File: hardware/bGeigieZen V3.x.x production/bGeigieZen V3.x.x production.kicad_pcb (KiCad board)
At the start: 2 copper layers, 129.4 x 64.6 mm, 17 parts, among them J1 M5 2x15 pin, J10 QI GND, J11 QI charger Plus, J2 Geiger IRover, J3 GPS, J4 Geiger Safepulse, J5 Extra support header, J6 Grove, J8 QI charger ground, J9 QI Plus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

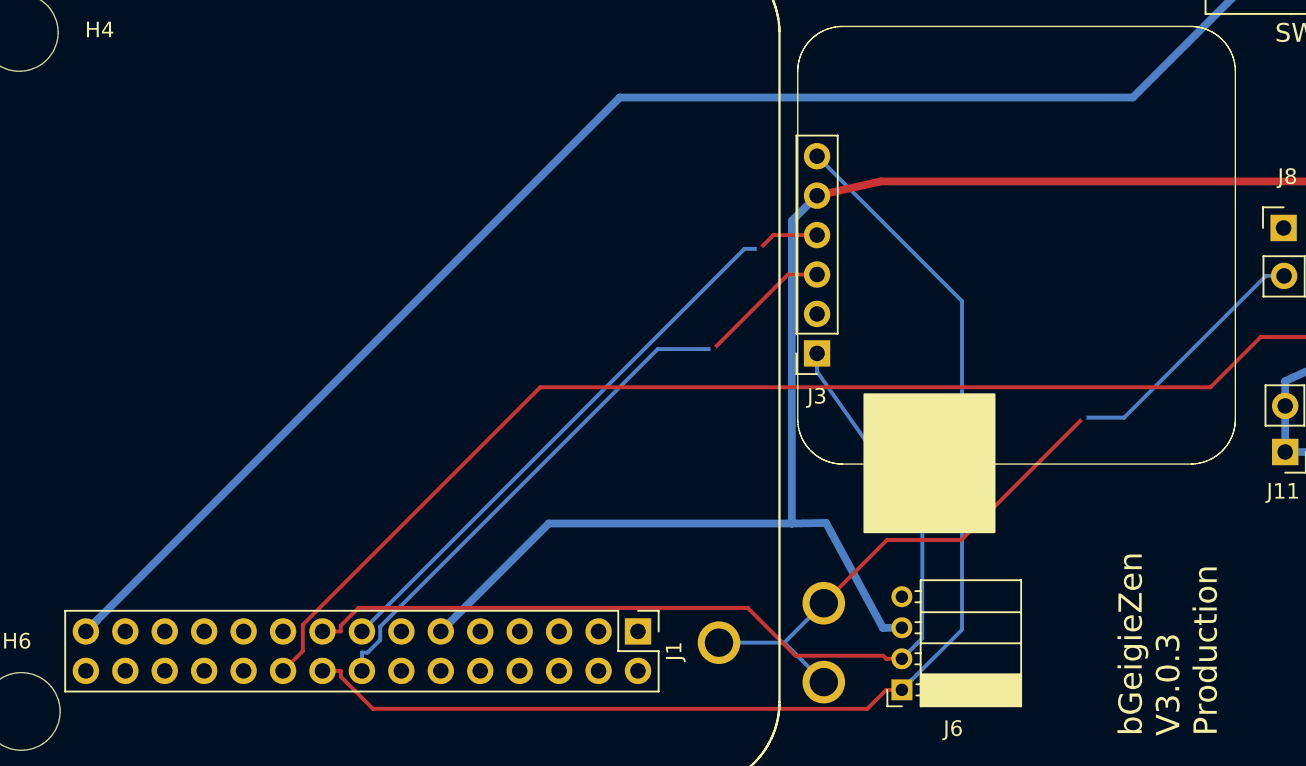
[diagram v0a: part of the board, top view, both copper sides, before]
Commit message: Cleaned up a lot of file. 4.0.1 was a bad board design. :(
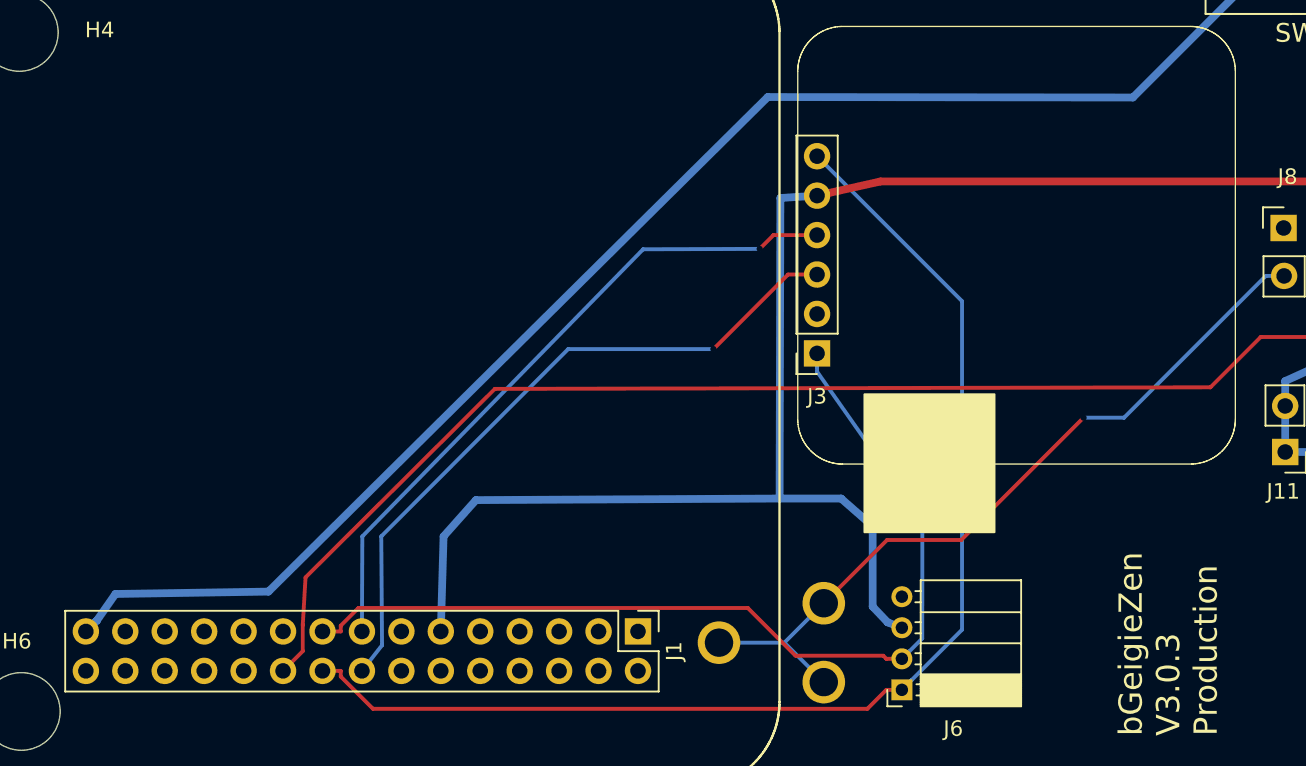
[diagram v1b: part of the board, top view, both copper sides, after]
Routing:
- net 3.3V: track 116.0 -> 122.4 mm
- net /RX2: track 39.9 -> 43.6 mm
- net /TX2: track 41.7 -> 45.1 mm
- net /GIO2 on Core and GIO32 on Core-2: track 107.8 -> 109.4 mm
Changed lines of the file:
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@@
 (kicad_pcb
-	(version 20240108)
+	(version 20240225)
 	(generator "pcbnew")
-	(generator_version "8.0")
+	(generator_version "8.99")
 	(general
 		(thickness 1.6)
@@
 	(segment
 		(start 149.29 91.7701)
-		(end 148.31 91.7701)
+		(end 141.7828 91.7944)
 		(width 0.25)
 		(layer "B.Cu")
@@
 	)
 	(segment
-		(start 123.6726 116.407)
+		(start 123.698 110.2856)
 		(end 123.673 116.407)
 		(width 0.25)
@@
 	)
 	(segment
-		(start 148.31 91.7701)
-		(end 123.673 116.407)
+		(start 123.673 116.407)
+		(end 123.6726 116.407)
+		(width 0.25)
+		(layer "B.Cu")
+		(net 2)
+	)
+	(segment
+		(start 141.7828 91.7944)
+		(end 123.698 110.2856)
 		(width 0.25)
 		(layer "B.Cu")
@@
 	)
 	(segment
-		(start 123.673 118.064)
-		(end 123.673 118.358)
-		(width 0.25)
-		(layer "B.Cu")
-		(net 3)
-	)
-	(segment
-		(start 146.31 98.2225)
-		(end 142.726 98.2225)
+		(start 124.968 117.296)
+		(end 123.6726 118.947)
 		(width 0.25)
 		(layer "B.Cu")
@@
 	)
 	(segment
-		(start 123.673 118.358)
+		(start 123.6726 118.947)
 		(end 123.673 118.6525)
 		(width 0.25)
@@
 	)
 	(segment
-		(start 142.726 98.2225)
-		(end 124.849 116.099)
-		(width 0.25)
-		(layer "B.Cu")
-		(net 3)
-	)
-	(segment
 		(start 123.673 118.6525)
 		(end 123.673 118.947)
@@
 	)
 	(segment
-		(start 124.04 117.77)
-		(end 123.673 117.77)
-		(width 0.25)
-		(layer "B.Cu")
-		(net 3)
-	)
-	(segment
-		(start 123.673 117.77)
-		(end 123.673 118.064)
-		(width 0.25)
-		(layer "B.Cu")
-		(net 3)
-	)
-	(segment
-		(start 124.849 116.961)
-		(end 124.04 117.77)
+		(start 123.673 118.6525)
+		(end 123.6726 118.6529)
 		(width 0.25)
 		(layer "B.Cu")
@@
 	)
 	(segment
-		(start 124.849 116.099)
-		(end 124.849 116.961)
+		(start 136.9568 98.2225)
+		(end 124.9172 110.2856)
 		(width 0.25)
 		(layer "B.Cu")
@@
 	)
 	(segment
-		(start 123.673 118.6525)
-		(end 123.6726 118.6529)
+		(start 146.31 98.2225)
+		(end 136.9568 98.2225)
 		(width 0.25)
 		(layer "B.Cu")
@@
 	)
 	(segment
-		(start 123.673 118.064)
-		(end 123.673 118.358)
+		(start 124.9172 110.2856)
+		(end 124.968 117.296)
 		(width 0.25)
 		(layer "B.Cu")
@@
 	)
 	(segment
-		(start 158.448 116.169)
-		(end 158.4476 116.169)
+		(start 152.985 88.34)
+		(end 152.985 88.3402)
 		(width 0.5)
 		(layer "B.Cu")
@@
 	)
 	(segment
-		(start 151.362 109.457)
-		(end 135.702 109.457)
+		(start 150.5712 107.8472)
+		(end 154.5336 107.8472)
 		(width 0.5)
 		(layer "B.Cu")
@@
 	)
 	(segment
-		(start 128.7526 116.407)
-		(end 128.753 116.407)
+		(start 158.448 116.169)
+		(end 158.4476 116.169)
 		(width 0.5)
 		(layer "B.Cu")
@@
 	)
 	(segment
-		(start 151.362 89.9626)
-		(end 151.362 109.457)
+		(start 128.753 116.407)
+		(end 128.7526 116.407)
 		(width 0.5)
 		(layer "B.Cu")
@@
 	)
 	(segment
-		(start 158.4476 116.169)
-		(end 157.226 116.1784)
+		(start 196.148 90.47)
+		(end 197.749 90.47)
 		(width 0.5)
 		(layer "B.Cu")
@@
 	)
 	(segment
-		(start 196.148 90.47)
-		(end 197.749 90.47)
+		(start 157.5308 115.8228)
+		(end 158.4476 116.169)
 		(width 0.5)
 		(layer "B.Cu")
@@
 	)
 	(segment
-		(start 135.702 109.457)
-		(end 128.753 116.407)
+		(start 156.5656 109.6252)
+		(end 156.5656 114.8068)
+		(width 0.5)
+		(layer "B.Cu")
+		(net 4)
+	)
+	(segment
+		(start 131.0132 107.9488)
+		(end 128.9304 110.2856)
 		(width 0.5)
 		(layer "B.Cu")
@@
 	)
 	(segment
-		(start 157.226 116.1784)
-		(end 153.5684 109.422)
+		(start 150.5712 107.8472)
+		(end 131.0132 107.9488)
 		(width 0.5)
 		(layer "B.Cu")
@@
 	)
 	(segment
-		(start 152.985 88.34)
-		(end 152.985 88.3402)
+		(start 154.5336 107.8472)
+		(end 156.5656 109.6252)
 		(width 0.5)
 		(layer "B.Cu")
@@
 	)
 	(segment
-		(start 153.5684 109.422)
-		(end 151.362 109.457)
+		(start 152.9846 88.34)
+		(end 152.985 88.34)
 		(width 0.5)
 		(layer "B.Cu")
@@
 	)
 	(segment
-		(start 196.148 90.47)
-		(end 196.1476 90.47)
+		(start 150.622 88.4924)
+		(end 150.5712 107.8472)
 		(width 0.5)
 		(layer "B.Cu")
@@
 	)
 	(segment
-		(start 152.985 88.3402)
-		(end 151.362 89.9626)
+		(start 128.9304 110.2856)
+		(end 128.753 116.407)
 		(width 0.5)
 		(layer "B.Cu")
@@
 	)
 	(segment
-		(start 152.9846 88.34)
-		(end 152.985 88.34)
+		(start 196.148 90.47)
+		(end 196.1476 90.47)
+		(width 0.5)
+		(layer "B.Cu")
+		(net 4)
+	)
+	(segment
+		(start 156.5656 114.8068)
+		(end 157.5308 115.8228)
 		(width 0.5)
 		(layer "B.Cu")
@@
 	)
 	(segment
+		(start 152.985 88.3402)
+		(end 150.622 88.4924)
+		(width 0.5)
+		(layer "B.Cu")
+		(net 4)
+	)
+	(segment
 		(start 207.916 117.14)
 		(end 207.9258 117.1498)
@@
 	)
 	(segment
-		(start 181.5572 97.4441)
-		(end 178.3169 100.6844)
+		(start 196.8472 97.4441)
+		(end 181.5572 97.4441)
 		(width 0.25)
 		(layer "F.Cu")
@@
 	)
 	(segment
-		(start 196.8472 97.4441)
-		(end 181.5572 97.4441)
-		(width 0.25)
-		(layer "F.Cu")
-		(net 19)
-	)
-	(segment
-		(start 119.8626 117.677)
-		(end 118.5926 118.947)
+		(start 119.8626 115.9833)
+		(end 119.8626 117.677)
 		(width 0.25)
 		(layer "F.Cu")
@@
 	)
 	(segment
+		(start 120.0404 112.9272)
+		(end 119.8626 115.9833)
+		(width 0.25)
+		(layer "F.Cu")
+		(net 19)
+	)
+	(segment
 		(start 198.1262 96.1651)
 		(end 193.608 91.6467)
@@
 	)
 	(segment
+		(start 119.8626 117.677)
+		(end 118.5926 118.947)
+		(width 0.25)
+		(layer "F.Cu")
+		(net 19)
+	)
+	(segment
 		(start 193.608 91.3521)
 		(end 193.608 91.0583)
@@
 	)
 	(segment
+		(start 198.1262 96.1651)
+		(end 196.8472 97.4441)
+		(width 0.25)
+		(layer "F.Cu")
+		(net 19)
+	)
+	(segment
 		(start 193.608 90.7641)
 		(end 193.6076 90.7637)
@@
 	)
 	(segment
-		(start 178.3169 100.6844)
-		(end 135.1615 100.6844)
-		(width 0.25)
-		(layer "F.Cu")
-		(net 19)
-	)
-	(segment
 		(start 199.831 97.87)
 		(end 198.1262 96.1651)
@@
 	)
 	(segment
-		(start 135.1615 100.6844)
-		(end 119.8626 115.9833)
+		(start 132.2324 100.786)
+		(end 120.0404 112.9272)
 		(width 0.25)
 		(layer "F.Cu")
@@
 	)
 	(segment
-		(start 198.1262 96.1651)
-		(end 196.8472 97.4441)
+		(start 178.3169 100.6844)
+		(end 132.2324 100.786)
 		(width 0.25)
 		(layer "F.Cu")
@@
 	)
 	(segment
-		(start 119.8626 115.9833)
-		(end 119.8626 117.677)
+		(start 181.5572 97.4441)
+		(end 178.3169 100.6844)
 		(width 0.25)
 		(layer "F.Cu")
@@
 	)
 	(segment
-		(start 140.28 82.02)
-		(end 106.613 115.687)
+		(start 149.8092 81.99)
+		(end 117.6528 113.8416)
 		(width 0.5)
 		(layer "B.Cu")
@@
 	)
 	(segment
+		(start 107.7976 113.994)
+		(end 106.613 115.687)
+		(width 0.5)
+		(layer "B.Cu")
+		(net 30)
+	)
+	(segment
 		(start 106.0725 116.227)
 		(end 105.9828 116.317)
@@
 	)
 	(segment
-		(start 181.506 73.8382)
-		(end 181.506 73.8384)
+		(start 181.506 73.8384)
+		(end 173.324 82.02)
+		(width 0.5)
+		(layer "B.Cu")
+		(net 30)
+	)
+	(segment
+		(start 117.6528 113.8416)
+		(end 107.7976 113.994)
 		(width 0.5)
 		(layer "B.Cu")
@@
 	)
 	(segment
+		(start 173.324 82.02)
+		(end 149.8092 81.99)
+		(width 0.5)
+		(layer "B.Cu")
+		(net 30)
+	)
+	(segment
 		(start 106.613 115.687)
 		(end 106.612 115.687)
@@
 	)
 	(segment
-		(start 173.324 82.02)
-		(end 140.28 82.02)
+		(start 181.506 73.8382)
+		(end 181.506 73.8384)
 		(width 0.5)
 		(layer "B.Cu")
@@
 		(width 0.5)
 		(layer "B.Cu")
-		(net 30)
-	)
-	(segment
-		(start 181.506 73.8384)
-		(end 173.324 82.02)
-		(width 0.5)
-		(layer "B.Cu")

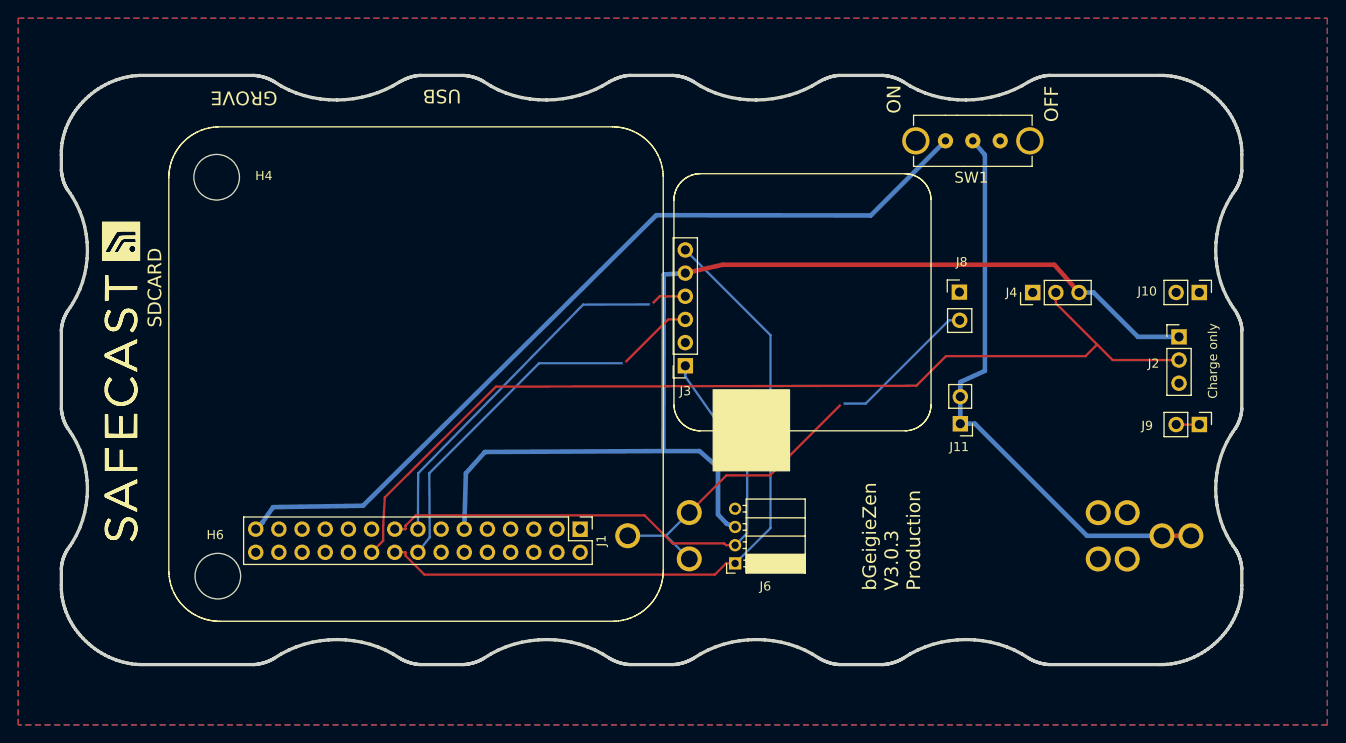
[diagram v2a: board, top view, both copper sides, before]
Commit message: Changed the 18650 battery holder to a 1043 Keystone and modified the layout.
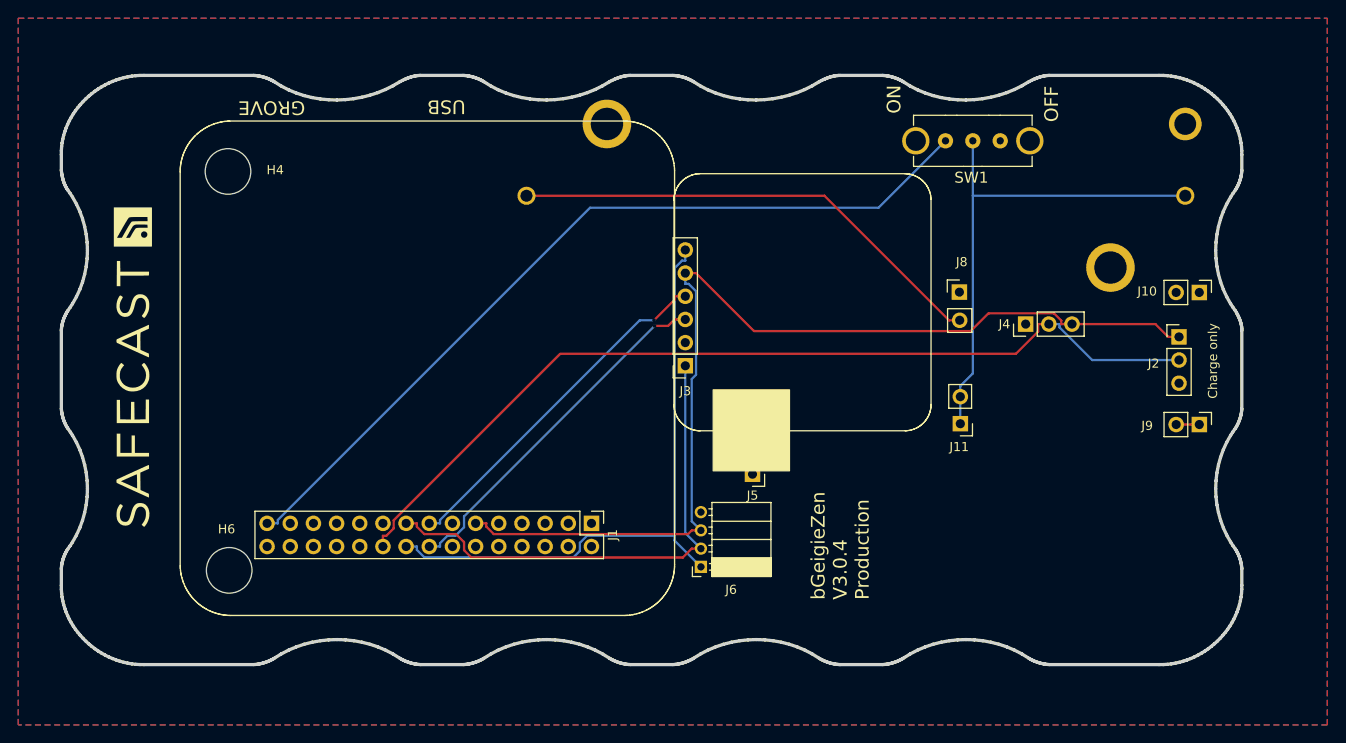
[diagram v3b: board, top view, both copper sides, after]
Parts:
- removed G***: LOGO, bGeigieZen:LOGO
- BT1: footprint Library:BATTERY_18650-HOLDER -> bGeigieZen:1043
- moved BT1 48.2 mm to (207.8, 79.9), turned to 0 degrees
- moved G back 3.83 mm to (92.4, 99.3)
- moved J6 3.77 mm to (154.7, 120.5)
- moved J4 3.54 mm to (190.3, 93.9)
- moved J5 3.54 mm to (160.4, 110.4)
- moved G front 2.04 mm to (92.4, 98.7)
- moved J1 1.40 mm to (142.7, 115.8)
- moved H6 1.40 mm to (103.0, 120.9)
- moved H4 1.40 mm to (102.9, 77.2)
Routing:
- net /SCL: track 79.3 -> 68.3 mm
- net /GIO2 on Core and GIO32 on Core-2: track 109.4 -> 100.9 mm
- net 3.3V: track 122.4 -> 113.9 mm
- net /VBATT: track 63.2 -> 54.9 mm
- net /SDA: track 62.2 -> 55.8 mm
- net /TX2: track 45.1 -> 39.3 mm
- net /RX2: track 43.6 -> 38.8 mm
- net Net-(BT1--): track 49.8 -> 53.1 mm, vias 1 -> 0
- net /BAT: track 94.8 -> 92.0 mm
- net GND: vias 3 -> 0
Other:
- board text added: "bGeigieZen V3.0.4 Production"
- board text removed: "SDCARD"
- board text removed: "bGeigieZen V3.0.3 Production"

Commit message: Added more 3D model files
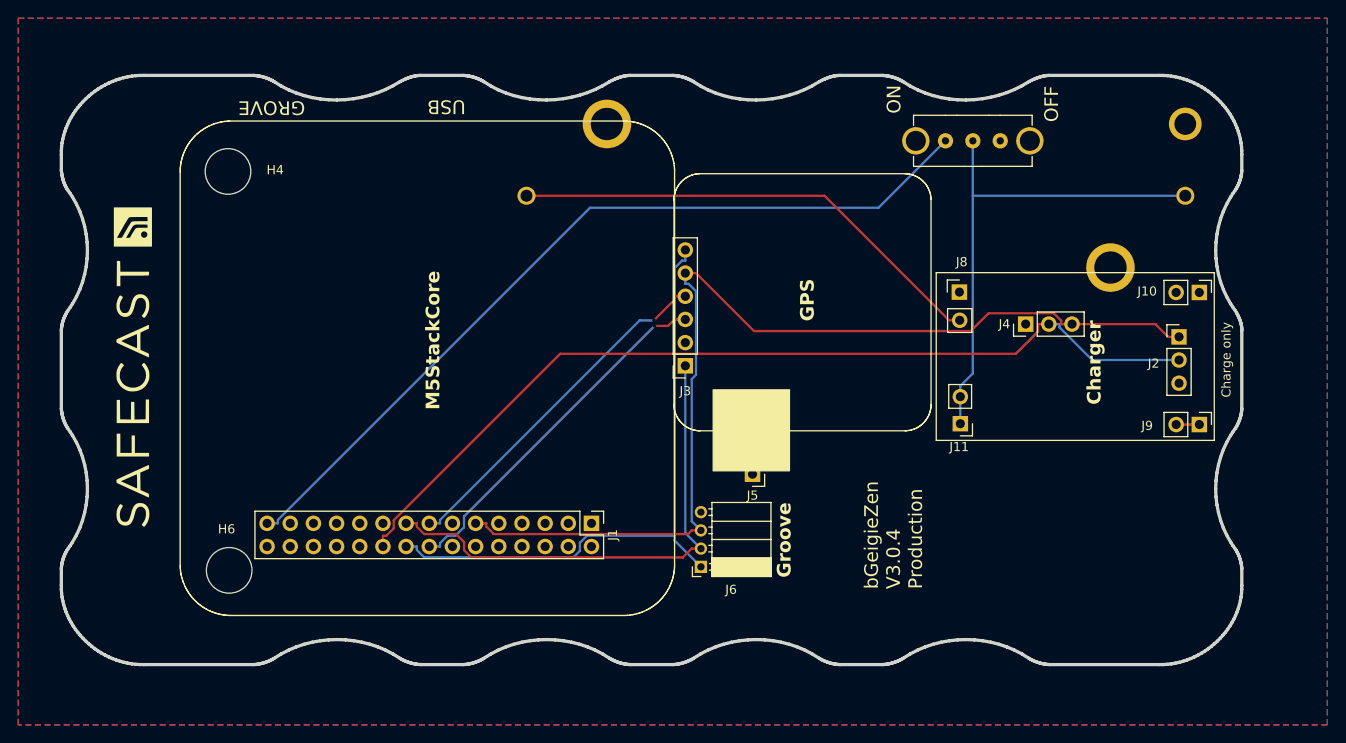
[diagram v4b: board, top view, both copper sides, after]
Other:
- board text added: "Charger"
- board text added: "Groove"
- board text added: "IRover pins"
- board text added: "M5StackCore"
- board text added: "SafePulse"
- board text added: "Safepulse pins"
- board text removed: "Safepulse"

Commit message: Updated SCL and SDA  and fixed labels  RXs and TX2
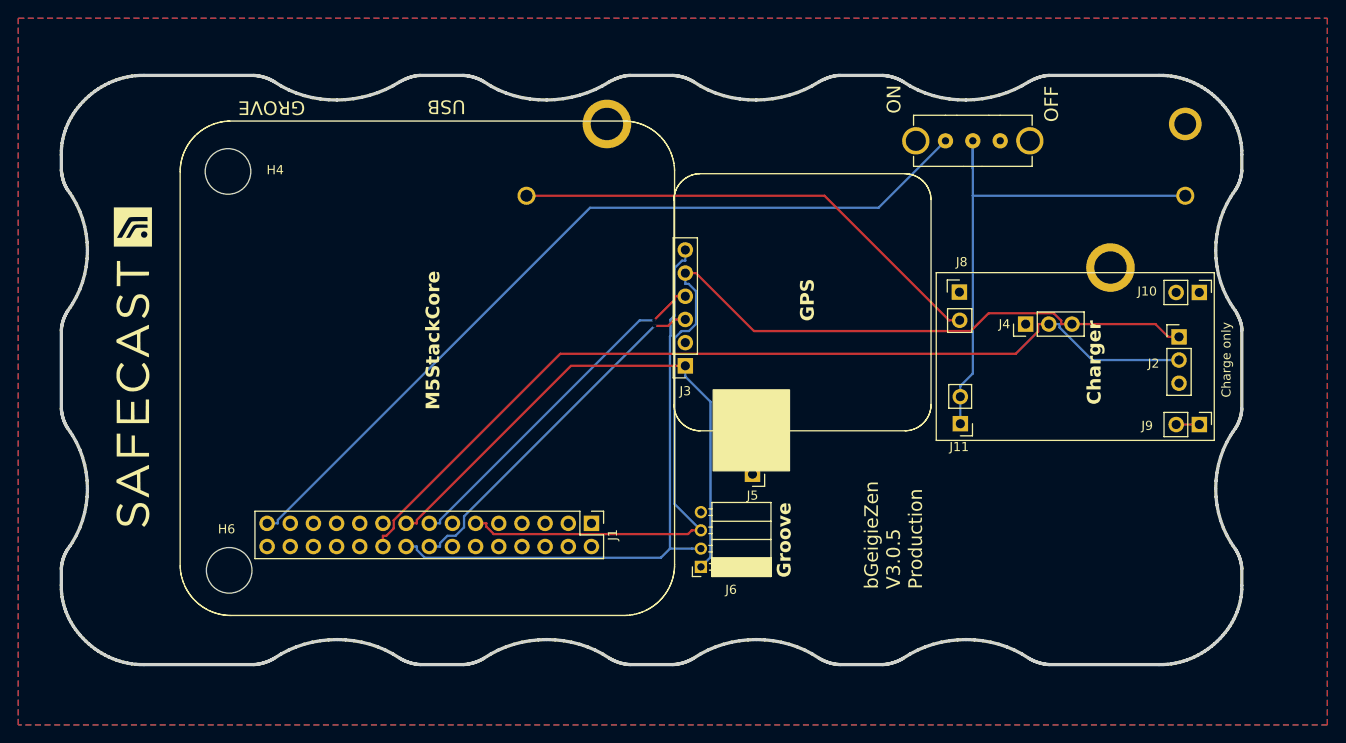
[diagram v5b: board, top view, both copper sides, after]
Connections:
- J1 pad 15: /RX2 -> /TX2
- J1 pad 16: /TX2 -> /RX2
- J1 pad 17: /SDA -> /SCL
- J1 pad 18: /SCL -> /SDA
- J3 pad 1: /SDA -> /SCL
- J3 pad 3: /TX2 -> /RX2
- J3 pad 4: /RX2 -> /TX2
- J3 pad 6: /SCL -> /SDA
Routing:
- net /SDA: track 55.8 -> 67.7 mm
- net /SCL: track 68.3 -> 61.6 mm
- net /VBATT: track 54.9 -> 57.9 mm
- net 3.3V: track 113.9 -> 116.3 mm
- net /GIO2 on Core and GIO32 on Core-2: track 100.9 -> 101.5 mm
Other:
- board text added: "bGeigieZen V3.0.5 Production"
